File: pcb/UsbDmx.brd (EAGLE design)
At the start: 22 parts, among them IC4 SN75176ASOIC, J2 POWER_JACKPTH, X1 USBPTH

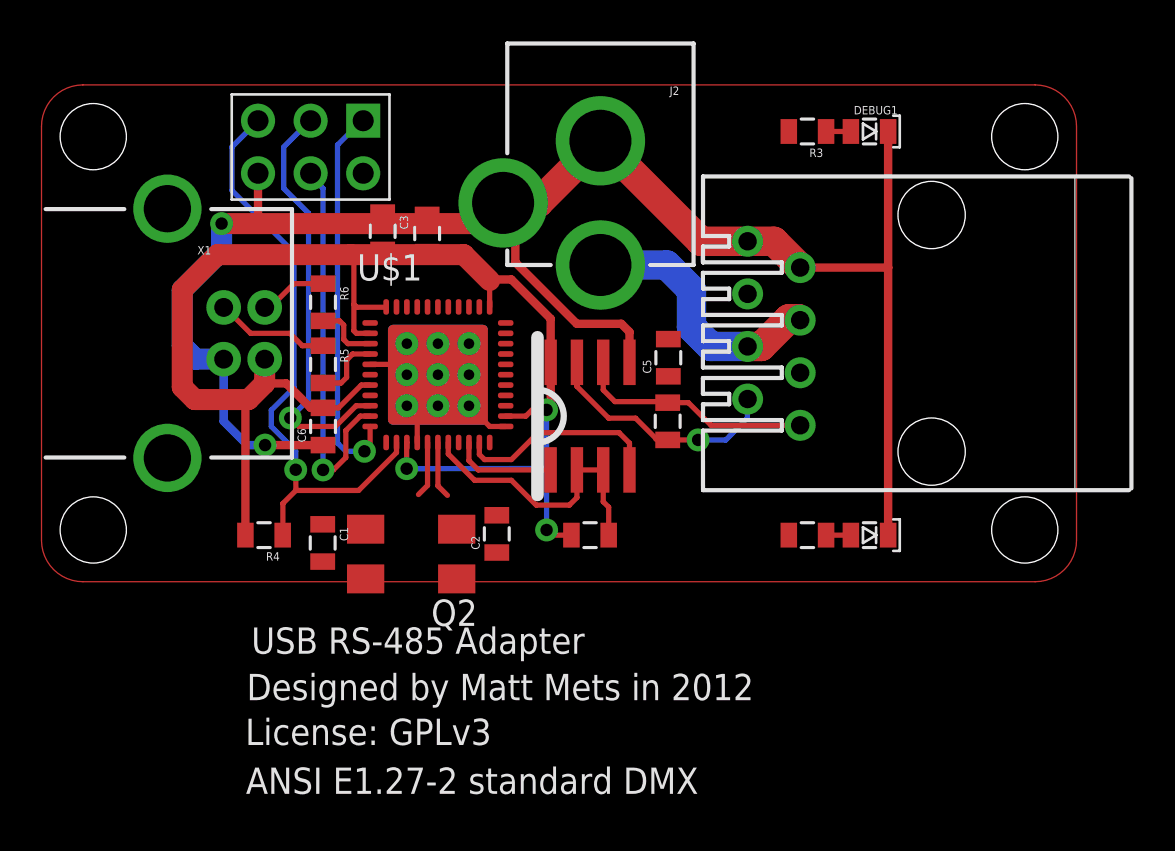
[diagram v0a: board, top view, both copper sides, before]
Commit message: Replaced crystal with smaller 3025 version, placed and routed all passives.
TODO: finish routing processor ground, final check, assemble BOM.
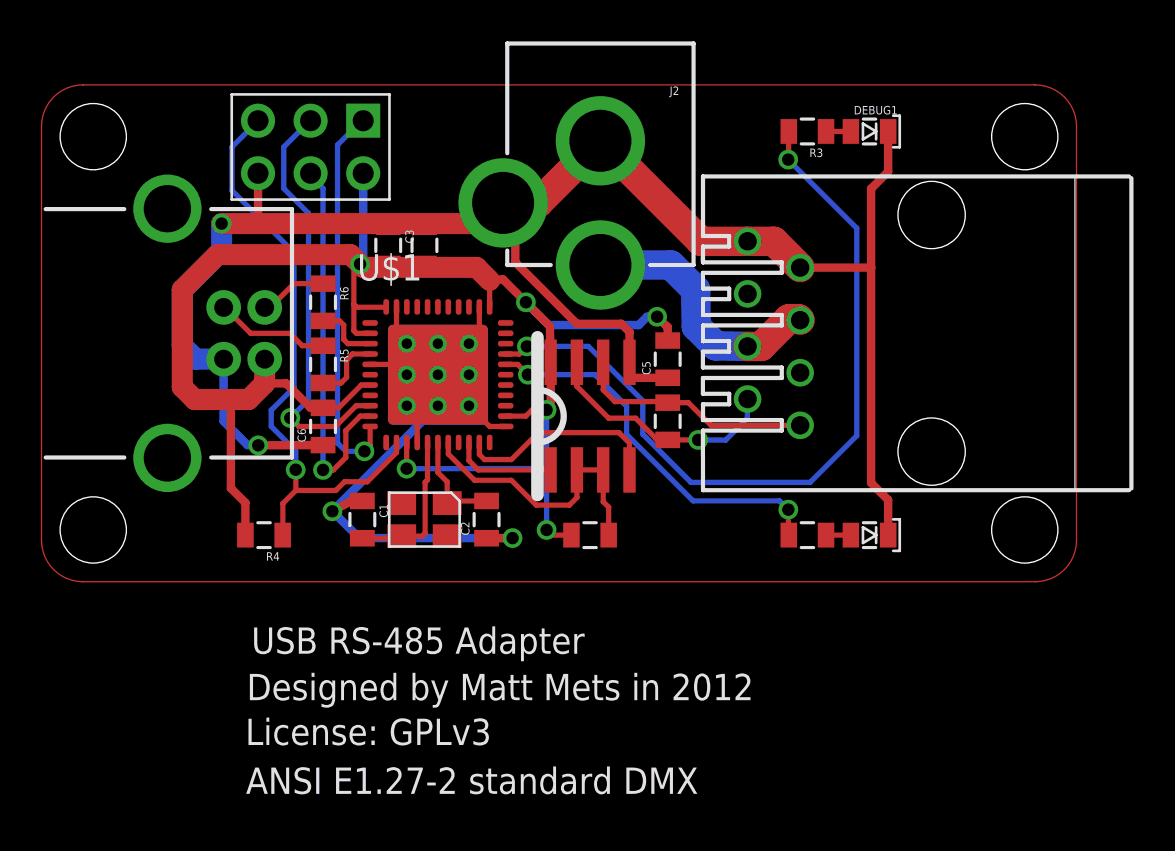
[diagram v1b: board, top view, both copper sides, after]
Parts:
- removed Q2: (no value), blinkyboard:GLOWBOARD_ABMM2_CRYSTAL
- added Q1: (no value), blinkyboard:XS3225
- moved C1 2.22 mm to (15.5, 3.00)
- moved C2 0.85 mm to (21.5, 3.00)
- moved C3 0.73 mm to (16.8, 16.2)
- moved C7 0.58 mm to (18.5, 16.2)
- moved C5 0.08 mm to (30.2, 10.8)
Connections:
- removed net D4: R3.2, R8.2
- new net D10: R3.2, U$1.30
- new net D9: R8.2, U$1.29
- net N$2: now also Q1.P$3; no longer Q2.P$3
- net N$5: now also Q1.P$1; no longer Q2.P$1
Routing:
- net D10: track 0.00 -> 37.8 mm, vias 0 -> 2
- net GND: track 98.5 -> 134.2 mm, vias 2 -> 4
- net D9: track 0.00 -> 18.6 mm, vias 0 -> 2
- net VCC: track 72.4 -> 88.5 mm, vias 3 -> 6
- net N$2: track 2.70 -> 7.57 mm
- net N$5: track 2.75 -> 5.05 mm

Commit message: Fixed processor thermal vias (no more DRC errors), finished ground routing, added missing UCAP
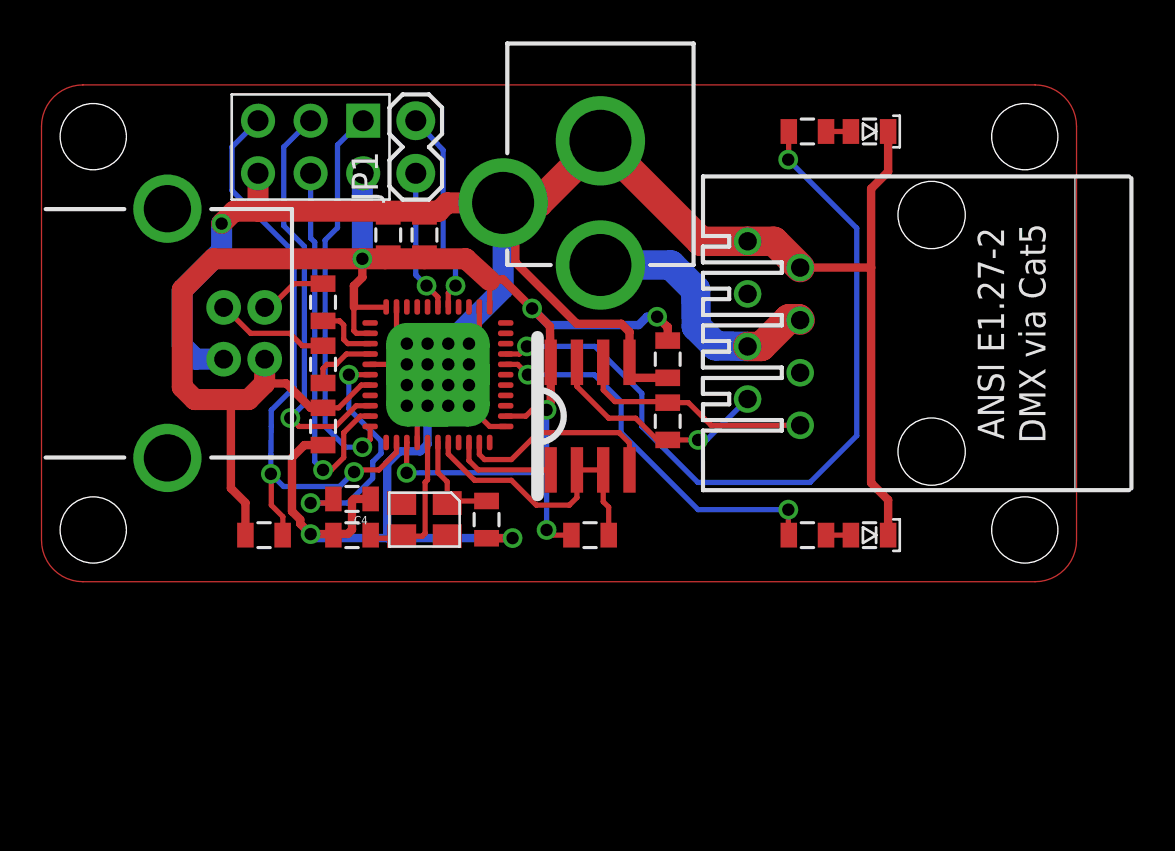
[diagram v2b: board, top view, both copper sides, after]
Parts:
- added C4: 1uF, SparkFun:0805
- added JP1: (no value), SparkFun:1X02
- DEBUG: value (none) -> RED
- DEBUG1: value (none) -> GREEN
- J1: value (none) -> RS485
- Q1: value (none) -> 16MHz 10ppm
- U$1: device blinkyboard:ARDUINO_LEONARDO-REV3B_SMARTPRJ_QFN44ML7X7 -> blinkiverse:ARDUINO_LEONARDO-REV3B_SMARTPRJ_QFN44ML7X7
- moved C1 0.90 mm to (15.0, 2.25), turned to 0 degrees
- moved C3 0.50 mm to (16.8, 16.8)
- moved C7 0.50 mm to (18.5, 16.8)
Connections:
- removed net D2: U$1.19
- new net A2: JP1.2, U$1.38
- new net A3: JP1.1, U$1.39
- new net N$9: C4.2, U$1.6
- net GND: now also C4.1, U$1.PAD@1, U$1.PAD@10, U$1.PAD@11, U$1.PAD@12, U$1.PAD@13, U$1.PAD@14, U$1.PAD@15, U$1.PAD@16, U$1.PAD@2, U$1.PAD@3, U$1.PAD@4, U$1.PAD@5, U$1.PAD@6, U$1.PAD@7, U$1.PAD@8, U$1.PAD@9; no longer U$1.EXP
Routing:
- net N$9: track 0.00 -> 11.6 mm, vias 0 -> 2
- net A2: track 0.00 -> 9.94 mm, vias 0 -> 1
- net GND: track 134.2 -> 143.1 mm, vias 4 -> 3
- net A3: track 0.00 -> 6.90 mm, vias 0 -> 1
- net VCC: track 88.5 -> 85.2 mm
- net RESET: track 29.1 -> 30.0 mm, vias 1 -> 2
- net RS485B: track 11.8 -> 11.3 mm
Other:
- board text added: "ANSI E1.27-2"
- board text added: "DMX via Cat5"
- board text added: "Rev A"
- board text added: "USB-DMX"
- board text added: "blinkiverse.com"
- board text removed: "ANSI E1.27-2 standard DMX"
- board text removed: "Designed by Matt Mets in 2012"
- board text removed: "License: GPLv3"
- board text removed: "USB RS-485 Adapter"
